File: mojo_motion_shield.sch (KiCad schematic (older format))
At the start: 31 parts, among them J1 SERVO, J10 MSX, J11 MSX, J12 MSX, J13 MSX, J14 MOT, J15 MOT, J16 MOT, J17 MOT, J18 ENC, J19 ENC, J2 ANALOG, J20 ENC, J21 ENC, J3 POWER, J4 LVSEL, J5 HOST, J6 SPI0, J7 SPI1, P1 MOJO, U2 A4988, U3 A4988, U4 A4988, U5 A4988

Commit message: update 6xTB67S249FTG shield
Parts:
- removed C3, C4, C5: 100uf, Capacitors_THT:CP_Radial_D5.0mm_P2.50mm, symbol CP_Small
- removed J11, J12, J13: MSX, mojov3:Pin_Header_Straight_3x03_Pitch2.54mm, symbol Conn_01x09
- removed J14, J15, J16, J17: MOT, Pin_Headers:Pin_Header_Straight_1x04_Pitch2.54mm, symbol Conn_01x04
- removed J18, J19, J20, J21: ENC, Pin_Headers:Pin_Header_Straight_1x04_Pitch2.54mm, symbol Conn_01x04
- removed J4: LVSEL, Pin_Headers:Pin_Header_Straight_1x03_Pitch2.54mm, symbol Conn_01x03
- removed U3, U4, U5: A4988, mojov3:A4988, symbol A4988
- added C2, C3, C4, C5, C6: 100uf, Capacitors_THT:CP_Radial_D5.0mm_P2.50mm, symbol mojo_motion_shield-rescue:CP_Small
- added J10, J17, J18, J4, J8, J9: ENC, Connector_PinHeader_2.54mm:PinHeader_1x05_P2.54mm_Vertical, symbol Connector_Generic:Conn_01x05
- added J12, J13, J14, J15, J16: MSX, mojov3:Pin_Header_Straight_3x03_Pitch2.54mm, symbol mojo_motion_shield-rescue:Conn_01x09
- added J19: SSERIAL0, Connector_PinHeader_2.54mm:PinHeader_2x04_P2.54mm_Vertical, symbol mojo_motion_shield-rescue:Conn_02x04_Odd_Even
- added J20: SSERIAL1, Connector_PinHeader_2.54mm:PinHeader_2x04_P2.54mm_Vertical, symbol mojo_motion_shield-rescue:Conn_02x04_Odd_Even
- added U2, U3, U4, U5, U6: TB67S2X9FTG, mojov3:TB67S2X9FTG, symbol mojo:TB67S2X9FTG
- C1: renamed from C2; symbol CP_Small -> mojo_motion_shield-rescue:CP_Small
- J1, J2: symbol Conn_01x24 -> mojo_motion_shield-rescue:Conn_01x24
- J11: renamed from J10; symbol Conn_01x09 -> mojo_motion_shield-rescue:Conn_01x09
- J3, J5: symbol Conn_01x04 -> mojo_motion_shield-rescue:Conn_01x04
- J6, J7: symbol Conn_02x04_Odd_Even -> mojo_motion_shield-rescue:Conn_02x04_Odd_Even
- P1: symbol MOJO -> mojo:MOJO
- R1, R2, R3: symbol R_Small -> mojo_motion_shield-rescue:R_Small
- U1: renamed from U2; value A4988 -> TB67S2X9FTG; footprint mojov3:A4988 -> mojov3:TB67S2X9FTG; symbol A4988 -> mojo:TB67S2X9FTG
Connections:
- net YENCB is gone; now on net XSTEP: P1.58
- net ZENCA is gone; now on net ZSTEP: P1.95
- net ZENCB is gone; now on net SPI1_CLK: P1.93
- net +12V: now also C2.1, C3.1, C4.1, C5.1, C6.1, U2.9 (VMOT), U3.9 (VMOT), U4.9 (VMOT), U5.9 (VMOT), U6.9 (VMOT)
- net +3V3: now also J11.1 (Pin_1), J11.2 (Pin_2), J11.3 (Pin_3), J6.1 (Pin_1), J7.1 (Pin_1), J10.1 (Pin_1), J12.1 (Pin_1), J12.2 (Pin_2), J12.3 (Pin_3), J13.1 (Pin_1), J13.2 (Pin_2), J13.3 (Pin_3), J14.1 (Pin_1), J14.2 (Pin_2), J14.3 (Pin_3), J15.1 (Pin_1), J15.2 (Pin_2), J15.3 (Pin_3), J16.1 (Pin_1), J16.2 (Pin_2), J16.3 (Pin_3), J17.1 (Pin_1), J18.1 (Pin_1), J4.1 (Pin_1), J8.1 (Pin_1), J9.1 (Pin_1)
- net +5V: now also J19.1 (Pin_1), J19.2 (Pin_2), J20.1 (Pin_1), J20.2 (Pin_2)
- net ADIR: now also P1.6, U4.8 (DIR); no longer P1.105
- net ASTEP: now also P1.5, U4.7 (STEP); no longer P1.102
- net CS0: now also P1.66; no longer P1.116
- net CS1: now also P1.74; no longer P1.118
- net CS2: now also P1.78; no longer P1.120
- net GND: now also C2.2, C3.2, C4.2, C5.2, C6.2, J10.5 (Pin_5), J12.7 (Pin_7), J12.8 (Pin_8), J12.9 (Pin_9), J13.7 (Pin_7), J13.8 (Pin_8), J13.9 (Pin_9), J14.7 (Pin_7), J14.8 (Pin_8), J14.9 (Pin_9), J15.7 (Pin_7), J15.8 (Pin_8), J15.9 (Pin_9), J16.7 (Pin_7), J16.8 (Pin_8), J16.9 (Pin_9), J17.5 (Pin_5), J18.5 (Pin_5), J19.7 (Pin_7), J19.8 (Pin_8), J20.7 (Pin_7), J20.8 (Pin_8), J4.5 (Pin_5), J8.5 (Pin_5), J9.5 (Pin_5), U2.10 (GND), U2.16 (GND), U3.10 (GND), U3.16 (GND), U4.10 (GND), U4.16 (GND), U5.10 (GND), U5.16 (GND), U6.10 (GND), U6.16 (GND)
- net XDIR: now also P1.57; no longer P1.83
- net XSTEP: no longer P1.81
- net YDIR: now also P1.80, U2.8 (DIR); no longer P1.88
- net YSTEP: now also P1.81, U2.7 (STEP); no longer P1.85
- net ZDIR: now also P1.94, U3.8 (DIR); no longer P1.115
- net ZSTEP: now also U3.7 (STEP); no longer P1.112
- net ~MOTION: now reaches P1.1
- net ~MOTION: now also U1.1 (~EN), U2.1 (~EN), U3.1 (~EN), U4.1 (~EN), U5.1 (~EN), U6.1 (~EN)
- net BSTEP: now reaches P1.11
- net BSTEP: now also U5.7 (STEP)
- net BDIR: now reaches P1.12
- net BDIR: now also U5.8 (DIR)
- net SS1RX: now reaches P1.27
- net SS1RX: now also J20.4 (Pin_4), J20.6 (Pin_6)
- net SS1TX: now reaches P1.30
- net SS1TX: now also J20.3 (Pin_3), J20.5 (Pin_5)
- net CSTEP: now reaches P1.32
- net CSTEP: now also U6.7 (STEP)
- net CDIR: now reaches P1.33
- net CDIR: now also U6.8 (DIR)
- net SS0RX: now reaches P1.35
- net SS0RX: now also J19.4 (Pin_4), J19.6 (Pin_6)
- net SS0TX: now reaches P1.41
- net SS0TX: now also J19.3 (Pin_3), J19.5 (Pin_5)
- net ~ECO: now reaches P1.50
- net ~ECO: now also U1.6 (AGC), U2.6 (AGC), U3.6 (AGC), U4.6 (AGC), U5.6 (AGC), U6.6 (AGC)
- net XENC_I: now reaches P1.101
- net XENC_I: now also J4.4 (Pin_4)
- net ZENC_A: now reaches P1.104
- net ZENC_A: now also J9.2 (Pin_2)
- net ZENC_B: now reaches P1.111
- net ZENC_B: now also J9.3 (Pin_3)
- net ZENC_I: now reaches P1.114
- net ZENC_I: now also J9.4 (Pin_4)
- net CS3: now reaches P1.84
- net CS3: now also J7.3 (Pin_3)
- net CS4: now reaches P1.87
- net CS4: now also J7.5 (Pin_5)
- net CS5: now reaches P1.92
- net CS5: now also J7.7 (Pin_7)
- net XENC_A: now reaches P1.97
- net XENC_A: now also J4.2 (Pin_2)
- net XENC_B: now reaches P1.99
- net XENC_B: now also J4.3 (Pin_3)
- net SPI1_OUT: now reaches J7.4 (Pin_4)
- net SPI1_OUT: now also P1.85
- net SPI1_IN: now reaches J7.6 (Pin_6)
- net SPI1_IN: now also P1.88
- net SPI1_CLK: now reaches J7.8 (Pin_8)
- net at U1.5 (~RST): no longer U1.6 (~SLP)
- net AENCA renamed YENC_B
- net YENC_B: now also J8.3 (Pin_3)
- net AENCB renamed YENC_A
- net YENC_A: now also J8.2 (Pin_2)
- removed net LVTTL: J11.1 (Pin_1), J11.2 (Pin_2), J11.3 (Pin_3), J6.1 (Pin_1), J7.1 (Pin_1), U1.15 (VDD)
- net MISO renamed CENC_B
- net CENC_B: now also J18.3 (Pin_3); no longer J6.6 (Pin_6)
- net MOSI renamed CENC_A
- net CENC_A: now also J18.2 (Pin_2); no longer J6.4 (Pin_4)
- net SCK renamed CENC_I
- net CENC_I: now also J18.4 (Pin_4); no longer J6.8 (Pin_8)
- net XENCA renamed SPI0_CLK
- net SPI0_CLK: now also J6.8 (Pin_8)
- net XENCB renamed SPI0_IN
- net SPI0_IN: now also J6.6 (Pin_6)
- net YENCA renamed SPI0_OUT
- net SPI0_OUT: now also J6.4 (Pin_4)
- new net: J14.6 (Pin_6), U4.2 (DM0)
- new net: J14.5 (Pin_5), U4.3 (DM1)
- new net: J14.4 (Pin_4), U4.4 (DM2)
- new net: J12.6 (Pin_6), U2.2 (DM0)
- new net: J12.5 (Pin_5), U2.3 (DM1)
- new net: J12.4 (Pin_4), U2.4 (DM2)
- new net: J15.6 (Pin_6), U5.2 (DM0)
- new net: J15.5 (Pin_5), U5.3 (DM1)
- new net: J15.4 (Pin_4), U5.4 (DM2)
- new net: J13.6 (Pin_6), U3.2 (DM0)
- new net: J13.5 (Pin_5), U3.3 (DM1)
- new net: J13.4 (Pin_4), U3.4 (DM2)
- new net: J16.6 (Pin_6), U6.2 (DM0)
- new net: J16.5 (Pin_5), U6.3 (DM1)
- new net: J16.4 (Pin_4), U6.4 (DM2)
- new net AENC_A: J10.2 (Pin_2), P1.105
- new net AENC_B: J10.3 (Pin_3), P1.112
- new net AENC_I: J10.4 (Pin_4), P1.115
- new net BENC_A: J17.2 (Pin_2), P1.116
- new net BENC_B: J17.3 (Pin_3), P1.118
- new net BENC_I: J17.4 (Pin_4), P1.120
- new net YENC_I: J8.4 (Pin_4), P1.102
- no-connect marks 68 -> 67
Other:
- moved on the sheet: C1, J11, J6, J7, U1

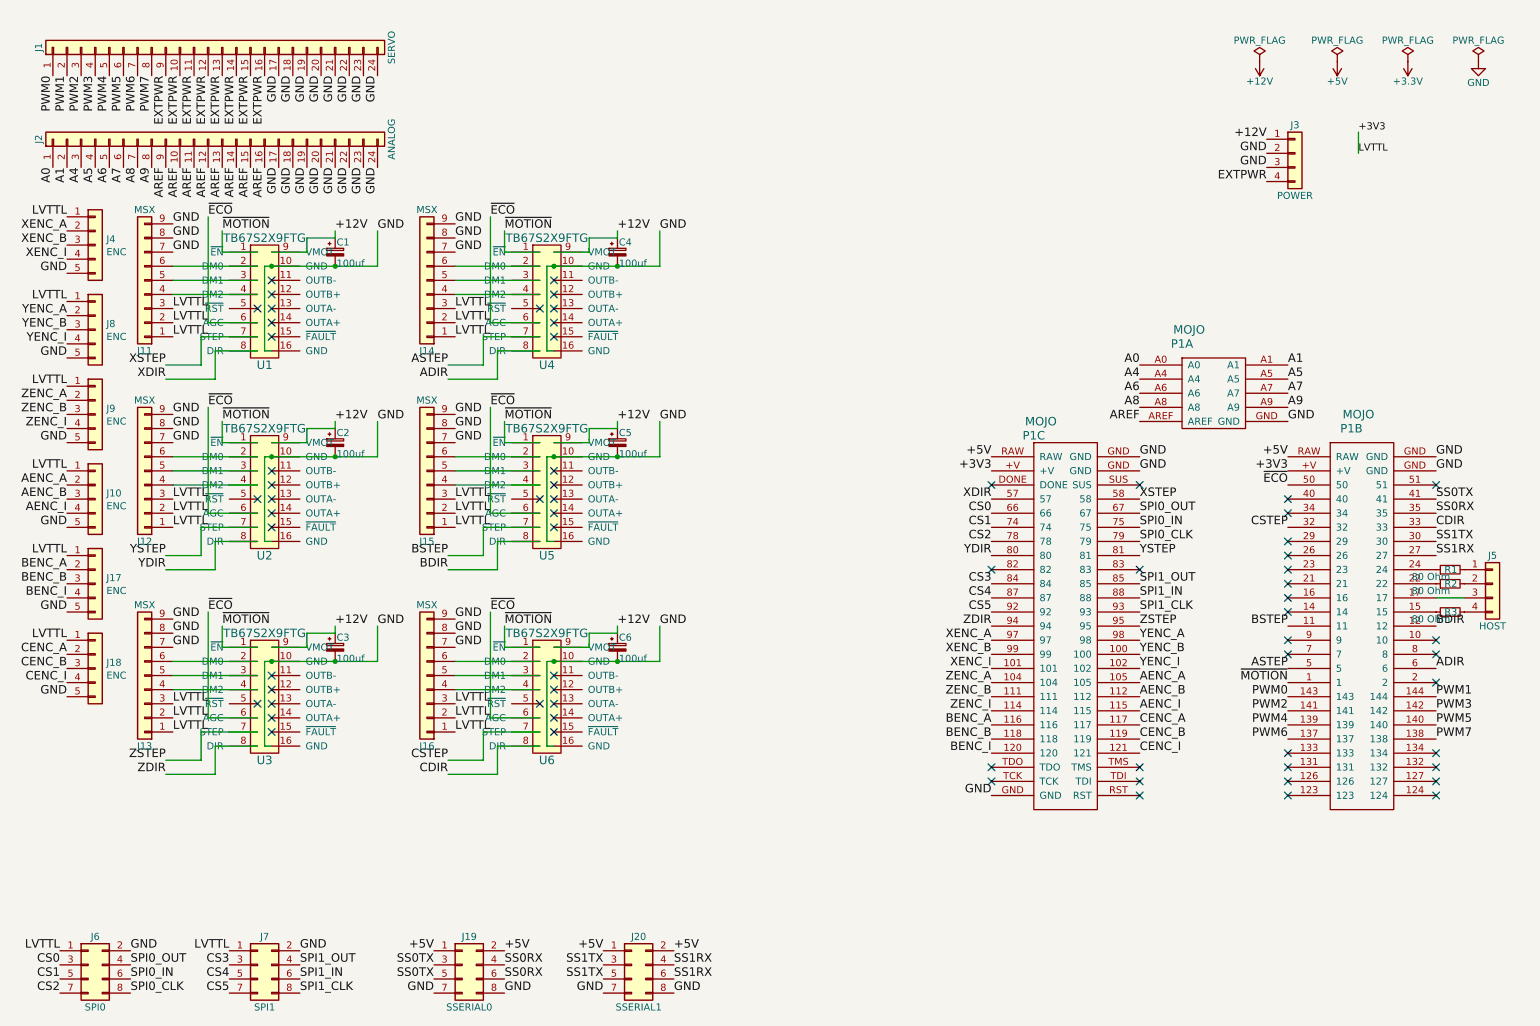
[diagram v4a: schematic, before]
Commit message: route fault pins from drivers to fpga
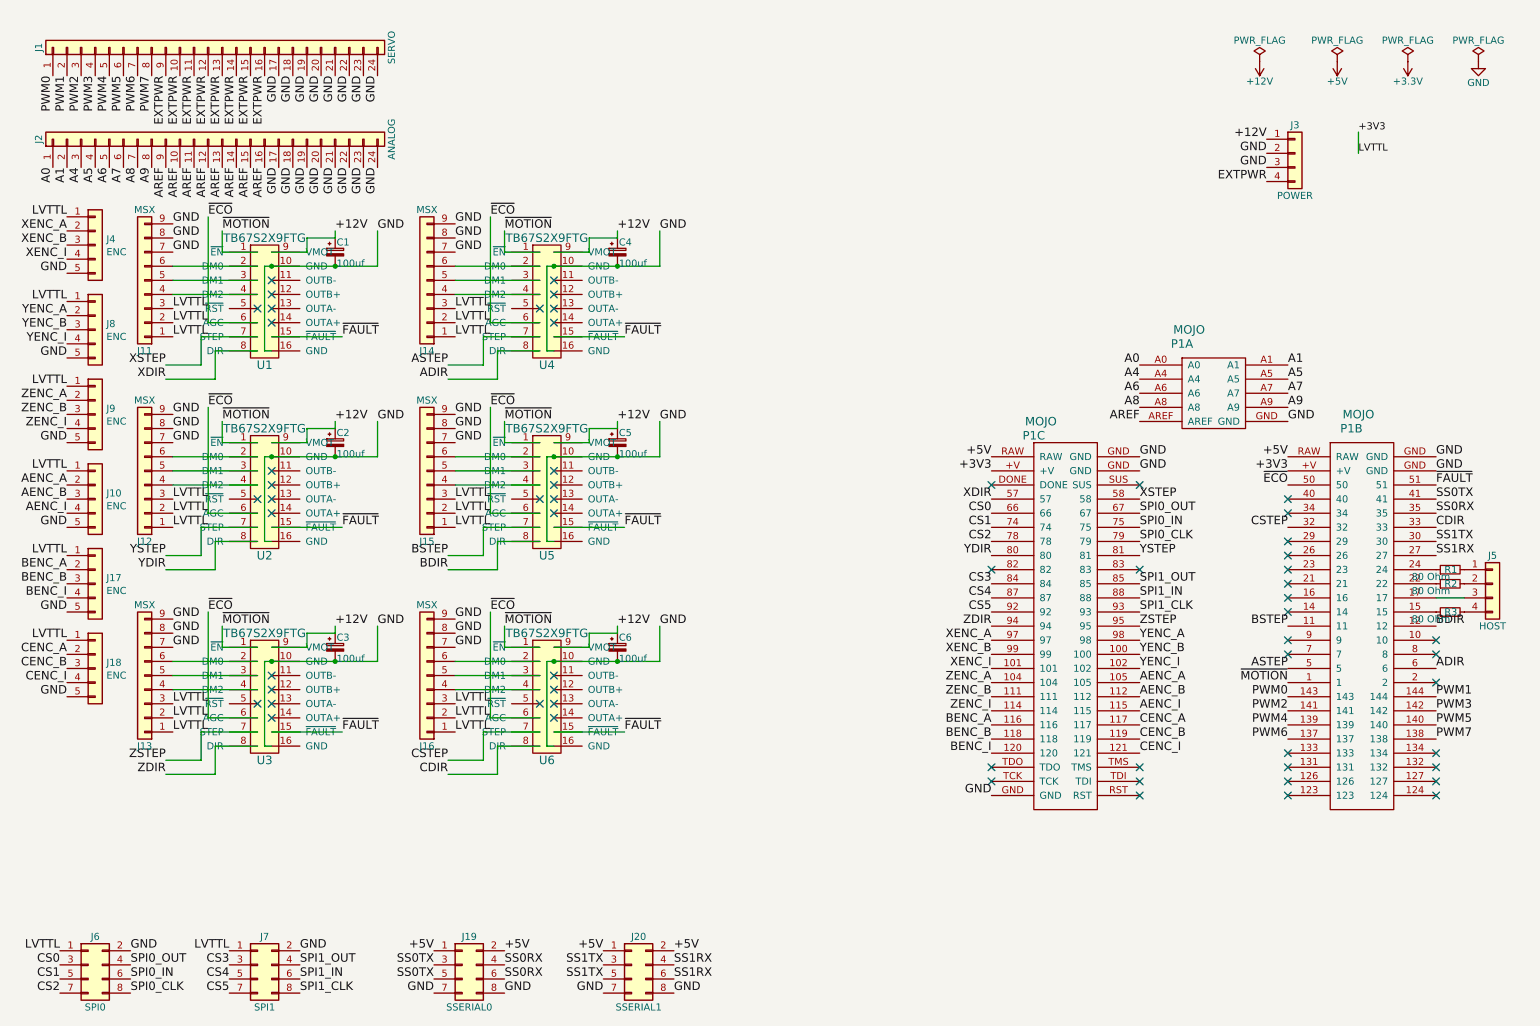
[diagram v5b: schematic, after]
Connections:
- net ~FAULT: now reaches P1.51
- net ~FAULT: now also U1.15 (~FAULT), U2.15 (~FAULT), U3.15 (~FAULT), U4.15 (~FAULT), U5.15 (~FAULT), U6.15 (~FAULT)
- no-connect marks 67 -> 60
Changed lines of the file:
@@
 NoConn ~ 2300 2800
 NoConn ~ 2200 2700
-NoConn ~ 2300 2900
 Text Label 9500 5350 2    60   ~ 0
 ~MOTION
@@
 NoConn ~ 4300 2800
 NoConn ~ 4200 2700
-NoConn ~ 4300 2900
 Text Label 3850 2050 0    60   ~ 0
 ~ECO
@@
 NoConn ~ 2300 4150
 NoConn ~ 2200 4050
-NoConn ~ 2300 4250
 Text Label 1850 3400 0    60   ~ 0
 ~ECO
@@
 NoConn ~ 4300 4150
 NoConn ~ 4200 4050
-NoConn ~ 4300 4250
 Text Label 3850 3400 0    60   ~ 0
 ~ECO
@@
 NoConn ~ 2300 5600
 NoConn ~ 2200 5500
-NoConn ~ 2300 5700
 Text Label 1850 4850 0    60   ~ 0
 ~ECO
@@
 NoConn ~ 4300 5600
 NoConn ~ 4200 5500
-NoConn ~ 4300 5700
 Text Label 3850 4850 0    60   ~ 0
 ~ECO
@@
 NoConn ~ 9500 4450
 NoConn ~ 9500 4350
-NoConn ~ 10550 3950
 NoConn ~ 9500 4050
 NoConn ~ 9500 4150
@@
 Text Label 10550 4150 0    60   ~ 0
 SS0RX
+Text Label 4800 2900 0    60   ~ 0
+~FAULT
+Text Label 4800 4250 0    60   ~ 0
+~FAULT
+Text Label 4800 5700 0    60   ~ 0
+~FAULT
+Text Label 2800 5700 0    60   ~ 0
+~FAULT
+Text Label 2800 4250 0    60   ~ 0
+~FAULT
+Text Label 2800 2900 0    60   ~ 0
+~FAULT
+Wire Wire Line
+	2300 2900 2800 2900
+Wire Wire Line
+	4300 2900 4800 2900
+Wire Wire Line
+	2300 4250 2800 4250
+Wire Wire Line
+	4300 4250 4800 4250
+Wire Wire Line
+	4300 5700 4800 5700
+Wire Wire Line
+	2300 5700 2800 5700
+Text Label 10550 3950 0    60   ~ 0
+~FAULT
 $EndSCHEMATC

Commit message: refactor port positions
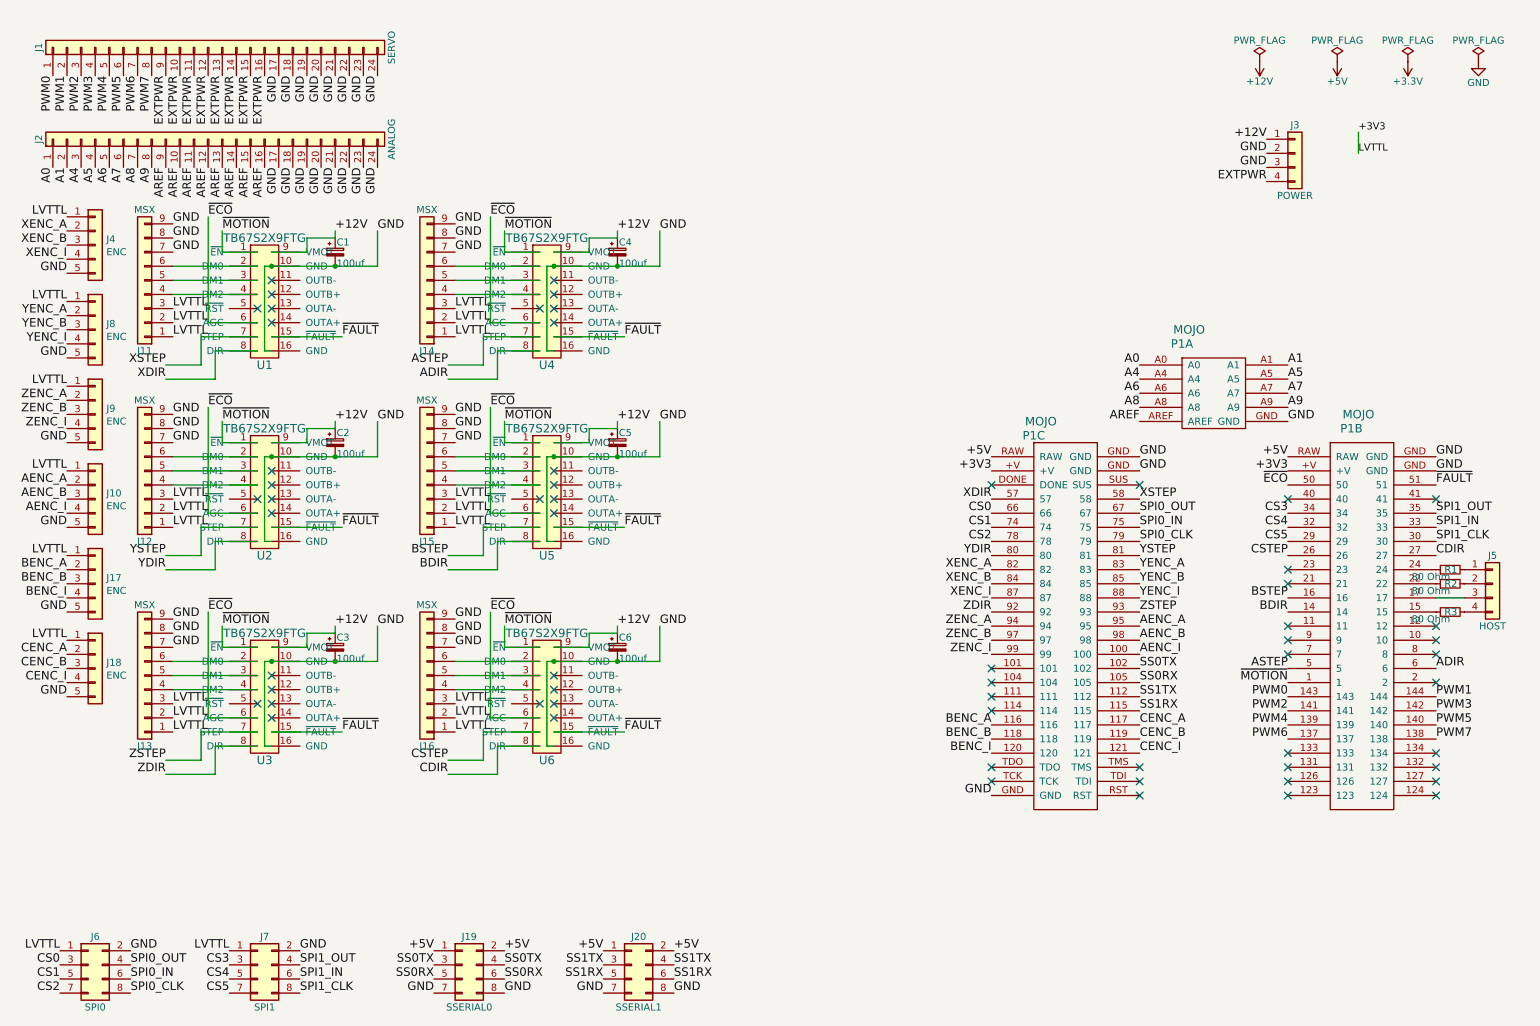
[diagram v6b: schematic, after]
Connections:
- net AENC_A: now also P1.95; no longer P1.105
- net AENC_B: now also P1.98; no longer P1.112
- net AENC_I: now also P1.100; no longer P1.115
- net BDIR: now also P1.14; no longer P1.12
- net BSTEP: now also P1.16; no longer P1.11
- net CDIR: now also P1.27; no longer P1.33
- net CS3: now also P1.34; no longer P1.84
- net CS4: now also P1.32; no longer P1.87
- net CS5: now also P1.29; no longer P1.92
- net CSTEP: now also P1.26; no longer P1.32
- net SPI1_CLK: now also P1.30; no longer P1.93
- net SPI1_IN: now also P1.33; no longer P1.88
- net SPI1_OUT: now also P1.35; no longer P1.85
- net SS0RX: now also J19.5 (Pin_5), P1.105; no longer J19.4 (Pin_4), P1.35
- net SS0TX: now also J19.4 (Pin_4), P1.102; no longer J19.5 (Pin_5), P1.41
- net SS1RX: now also J20.5 (Pin_5), P1.115; no longer J20.4 (Pin_4), P1.27
- net SS1TX: now also J20.4 (Pin_4), P1.112; no longer J20.5 (Pin_5), P1.30
- net XENC_A: now also P1.82; no longer P1.97
- net XENC_B: now also P1.84; no longer P1.99
- net XENC_I: now also P1.87; no longer P1.101
- net YENC_A: now also P1.83; no longer P1.98
- net YENC_B: now also P1.85; no longer P1.100
- net YENC_I: now also P1.88; no longer P1.102
- net ZDIR: now also P1.92; no longer P1.94
- net ZENC_A: now also P1.94; no longer P1.104
- net ZENC_B: now also P1.97; no longer P1.111
- net ZENC_I: now also P1.99; no longer P1.114
- net ZSTEP: now also P1.93; no longer P1.95
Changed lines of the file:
@@
 Text Label 7400 4450 2    60   ~ 0
 YDIR
-Text Label 7400 4950 2    60   ~ 0
+Text Label 7400 4850 2    60   ~ 0
 ZDIR
 Text Label 8450 4150 0    60   ~ 0
@@
 GND
 NoConn ~ 10550 5350
-NoConn ~ 10550 5150
-NoConn ~ 10550 5050
 NoConn ~ 2300 2500
 NoConn ~ 2300 2600
@@
 Text Label 10550 5250 0    60   ~ 0
 ADIR
-Text Label 9500 4950 2    60   ~ 0
+Text Label 9500 4750 2    60   ~ 0
 BSTEP
-Text Label 10550 4950 0    60   ~ 0
+Text Label 9500 4850 2    60   ~ 0
 BDIR
-Text Label 9500 4250 2    60   ~ 0
+Text Label 9500 4450 2    60   ~ 0
 CSTEP
-Text Label 10550 4250 0    60   ~ 0
+Text Label 10550 4450 0    60   ~ 0
 CDIR
 Wire Wire Line
@@
 Wire Wire Line
 	4750 5200 5050 5200
-Text Label 8450 4950 0    60   ~ 0
+Text Label 8450 4850 0    60   ~ 0
 ZSTEP
 Text Label 10000 1450 0    50   ~ 0
@@
 	1    0    0    -1
 $EndComp
-NoConn ~ 7400 4550
 Text Label 2000 7350 2    60   ~ 0
 CS3
@@
 Text Label 2500 7550 0    60   ~ 0
 SPI1_CLK
-Text Label 8450 4650 0    60   ~ 0
+Text Label 10550 4150 0    60   ~ 0
 SPI1_OUT
-Text Label 8450 4750 0    60   ~ 0
+Text Label 10550 4250 0    60   ~ 0
 SPI1_IN
-Text Label 8450 4850 0    60   ~ 0
+Text Label 10550 4350 0    60   ~ 0
 SPI1_CLK
-Text Label 7400 4650 2    60   ~ 0
+Text Label 9500 4150 2    60   ~ 0
 CS3
-Text Label 7400 4750 2    60   ~ 0
+Text Label 9500 4250 2    60   ~ 0
 CS4
-Text Label 7400 4850 2    60   ~ 0
+Text Label 9500 4350 2    60   ~ 0
 CS5
-NoConn ~ 8450 4550
-NoConn ~ 9500 5150
-NoConn ~ 9500 5050
-NoConn ~ 9500 4850
-NoConn ~ 9500 4750
 NoConn ~ 9500 4650
 NoConn ~ 9500 4550
-NoConn ~ 9500 4450
-NoConn ~ 9500 4350
-NoConn ~ 9500 4050
-NoConn ~ 9500 4150
 $Comp
 L Connector_Generic:Conn_01x05 J4
@@
 Text Label 850  5350 2    60   ~ 0
 CENC_I
+Text Label 8450 4550 0    60   ~ 0
+YENC_A
+Text Label 8450 4650 0    60   ~ 0
+YENC_B
+Text Label 8450 4750 0    60   ~ 0
+YENC_I
+Text Label 7400 4550 2    60   ~ 0
+XENC_A
+Text Label 7400 4650 2    60   ~ 0
+XENC_B
+Text Label 7400 4750 2    60   ~ 0
+XENC_I
+Text Label 7400 4950 2    60   ~ 0
+ZENC_A
+Text Label 7400 5050 2    60   ~ 0
+ZENC_B
+Text Label 7400 5150 2    60   ~ 0
+ZENC_I
+Text Label 8450 4950 0    60   ~ 0
+AENC_A
 Text Label 8450 5050 0    60   ~ 0
-YENC_A
+AENC_B
 Text Label 8450 5150 0    60   ~ 0
-YENC_B
-Text Label 8450 5250 0    60   ~ 0
-YENC_I
-Text Label 7400 5050 2    60   ~ 0
-XENC_A
-Text Label 7400 5150 2    60   ~ 0
-XENC_B
-Text Label 7400 5250 2    60   ~ 0
-XENC_I
-Text Label 7400 5350 2    60   ~ 0
-ZENC_A
-Text Label 7400 5450 2    60   ~ 0
-ZENC_B
-Text Label 7400 5550 2    60   ~ 0
-ZENC_I
-Text Label 8450 5350 0    60   ~ 0
-AENC_A
-Text Label 8450 5450 0    60   ~ 0
-AENC_B
-Text Label 8450 5550 0    60   ~ 0
 AENC_I
 Text Label 7400 6150 2    60   ~ 0
@@
 Text Label 3450 7350 2    60   ~ 0
 SS0TX
+Text Label 3950 7450 0    60   ~ 0
+SS0RX
+Text Label 3950 7350 0    60   ~ 0
+SS0TX
 Text Label 3450 7450 2    60   ~ 0
-SS0TX
-Text Label 3950 7350 0    60   ~ 0
-SS0RX
-Text Label 3950 7450 0    60   ~ 0
 SS0RX
 Text Label 4650 7350 2    60   ~ 0
 SS1TX
 Text Label 4650 7450 2    60   ~ 0
+SS1RX
+Text Label 5150 7350 0    60   ~ 0
 SS1TX
-Text Label 5150 7350 0    60   ~ 0
-SS1RX
 Text Label 5150 7450 0    60   ~ 0
 SS1RX
-Text Label 10550 4450 0    60   ~ 0
+Text Label 8450 5550 0    60   ~ 0
 SS1RX
-Text Label 10550 4350 0    60   ~ 0
+Text Label 8450 5450 0    60   ~ 0
 SS1TX
-Text Label 10550 4050 0    60   ~ 0
+Text Label 8450 5250 0    60   ~ 0
 SS0TX
-Text Label 10550 4150 0    60   ~ 0
+Text Label 8450 5350 0    60   ~ 0
 SS0RX
 Text Label 4800 2900 0    60   ~ 0
@@
 Text Label 10550 3950 0    60   ~ 0
 ~FAULT
+NoConn ~ 7400 5550
+NoConn ~ 7400 5450
+NoConn ~ 7400 5350
+NoConn ~ 7400 5250
+NoConn ~ 9500 5150
+NoConn ~ 9500 5050
+NoConn ~ 9500 4950
+NoConn ~ 10550 4950
+NoConn ~ 10550 5050
+NoConn ~ 10550 5150
+NoConn ~ 9500 4050
+NoConn ~ 10550 4050
 $EndSCHEMATC
